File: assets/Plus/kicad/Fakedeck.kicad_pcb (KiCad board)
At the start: 2 copper layers, 118.8 x 101.5 mm, 14 parts, among them J1 Conn_01x06_Pin, J2 Conn_01x06_Pin, SW1 RotaryEncoder_Switch, SW2 RotaryEncoder_Switch, SW3 RotaryEncoder_Switch, SW4 RotaryEncoder_Switch, U1 Pico, U2 ATtiny2313-20P

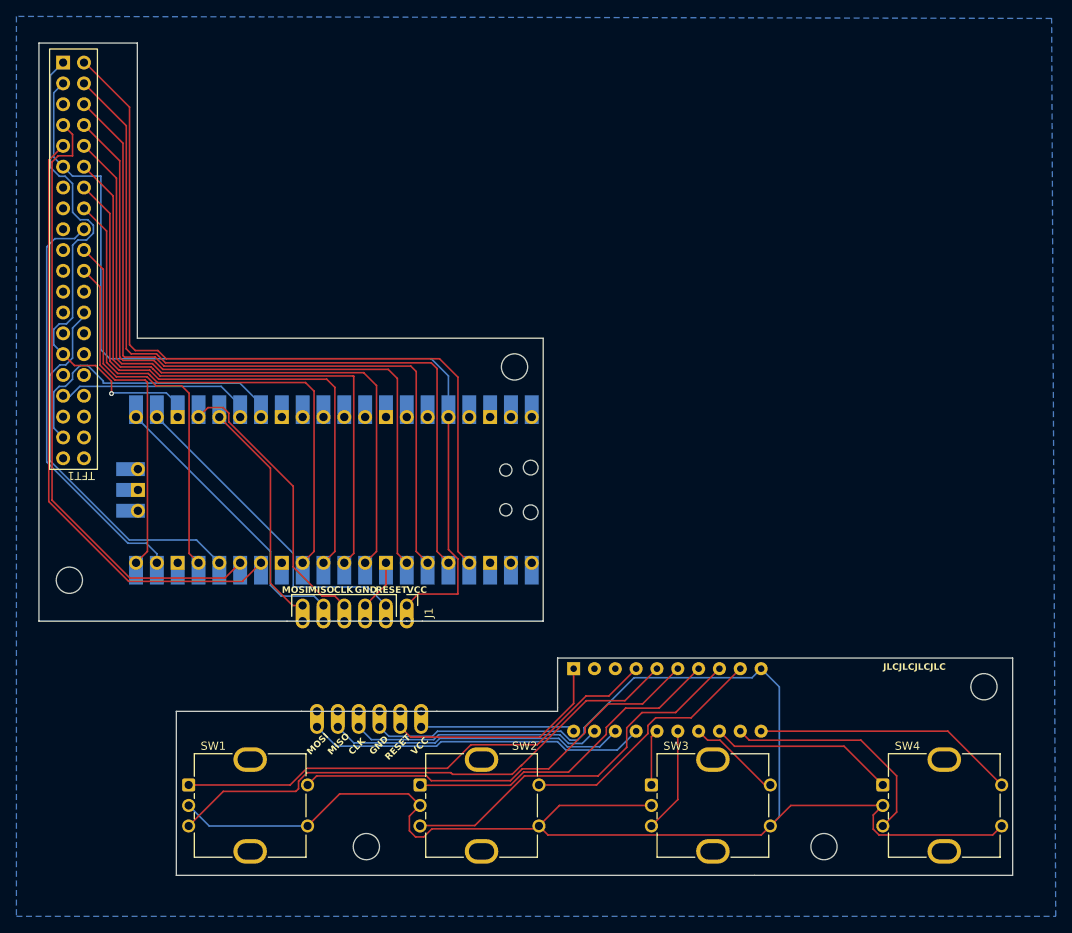
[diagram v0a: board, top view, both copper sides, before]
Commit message: Plus: Changed to connect the rotary encoder directly to the Pico. Removed the Attiny. - Updated the PCB.
 Co-Authored-By: Claude Sonnet 4.6 <noreply@anthropic.com>
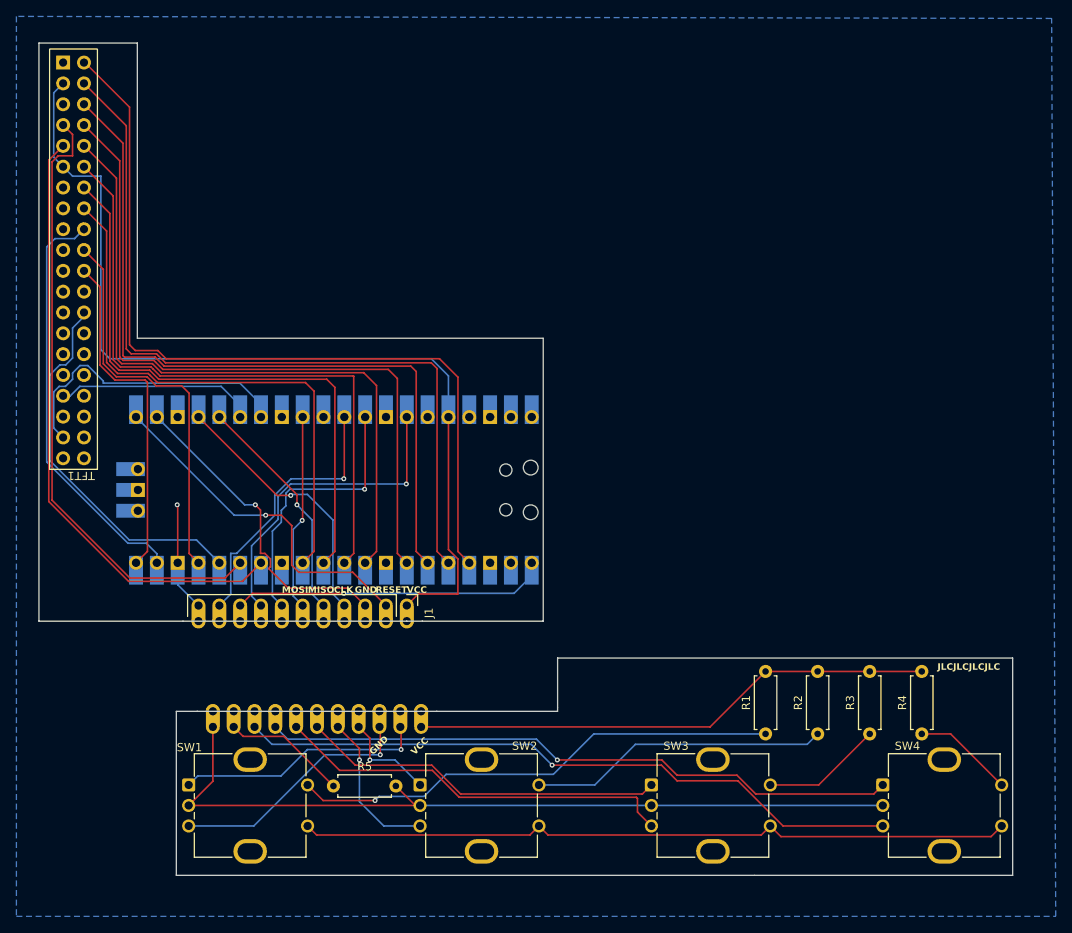
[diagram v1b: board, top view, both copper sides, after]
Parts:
- removed J2: Conn_01x06_Pin, Connector_Pin_2.54mm_Castellated:PinHeader_Castellated_1x06_P2.54mm_Vertical
- removed REF** (x5): MountingHole_3.2mm_M3, MountingHole:MountingHole_3.2mm_M3
- removed U2: ATtiny2313-20P, Package_DIP:DIP-20_W7.62mm
- added J3: Conn_01x11_Pin, Connector_Pin_2.54mm_Castellated:PinHeader_Castellated_1x11_P2.54mm_Vertical, B.Cu at (147.9, 134.4)
- added R1: 120, Resistor_THT:R_Axial_DIN0207_L6.3mm_D2.5mm_P7.62mm_Horizontal, F.Cu at (189.9, 135.3)
- added R2: 220, Resistor_THT:R_Axial_DIN0207_L6.3mm_D2.5mm_P7.62mm_Horizontal, F.Cu at (196.2, 135.3)
- added R3: 470, Resistor_THT:R_Axial_DIN0207_L6.3mm_D2.5mm_P7.62mm_Horizontal, F.Cu at (202.6, 135.3)
- added R4: 1K, Resistor_THT:R_Axial_DIN0207_L6.3mm_D2.5mm_P7.62mm_Horizontal, F.Cu at (208.9, 135.3)
- added R5: 47, Resistor_THT:R_Axial_DIN0207_L6.3mm_D2.5mm_P7.62mm_Horizontal, F.Cu at (137.2, 141.6)
- J1: value Conn_01x06_Pin -> Conn_01x11_Pin; footprint Connector_Pin_2.54mm_Castellated:PinHeader_Castellated_1x06_P2.54mm_Vertical -> Connector_Pin_2.54mm_Castellated:PinHeader_Castellated_1x11_P2.54mm_Vertical
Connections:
- J1 pad 2: /AT_RESET -> /RE1_A
- J1 pad 3: TFT_CS -> /RE1_B
- J1 pad 4: /AT_CLK -> /RE2_A
- J1 pad 5: /AT_MISO -> /RE2_B
- J1 pad 6: /AT_MOSI -> /RE3_A
- SW1 pad C: TFT_CS -> GND
- SW1 pad S1: /RE1_S -> Net-(R1-Pad1)
- SW1 pad S2: TFT_CS -> /RE_SW
- SW2 pad C: TFT_CS -> GND
- SW2 pad S1: /RE2_S -> Net-(R2-Pad1)
- SW2 pad S2: TFT_CS -> /RE_SW
- SW3 pad C: TFT_CS -> GND
- SW3 pad S1: /RE3_S -> Net-(R3-Pad1)
- SW3 pad S2: TFT_CS -> /RE_SW
- SW4 pad C: TFT_CS -> GND
- SW4 pad S1: /RE4_S -> Net-(R4-Pad1)
- SW4 pad S2: TFT_CS -> /RE_SW
- TFT1 pad 1: TFT_CS -> GND
- TFT1 pad 15: TFT_CS -> GND
- U1 pad 1: unconnected-(U1-GPIO0-Pad1) -> /RE4_B
- U1 pad 18: unconnected-(U1-GND-Pad18)_1 -> GND
- U1 pad 21: /AT_MISO -> /RE1_A
- U1 pad 22: /AT_RESET -> /RE1_B
- U1 pad 23: TFT_CS -> GND
- U1 pad 24: /AT_CLK -> /RE2_A
- U1 pad 25: /AT_MOSI -> /RE2_B
- U1 pad 29: unconnected-(U1-GPIO22-Pad29)_1 -> /RE3_A
- U1 pad 3: unconnected-(U1-GND-Pad3)_1 -> GND
- U1 pad 31: unconnected-(U1-GPIO26_ADC0-Pad31)_1 -> /RE_SW
- U1 pad 32: unconnected-(U1-GPIO27_ADC1-Pad32)_1 -> /RE3_B
- U1 pad 34: unconnected-(U1-GPIO28_ADC2-Pad34)_1 -> /RE4_A
- U1 pad 8: TFT_CS -> GND
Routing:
- net TFT_CS: track 270.7 -> 0.00 mm, vias 1 -> 0
- net /RE_SW: track 0.00 -> 136.2 mm, vias 0 -> 1
- net GND: track 0.00 -> 113.3 mm, vias 0 -> 1
- net /RE4_A: track 22.6 -> 117.5 mm, vias 0 -> 2
- net /RE4_B: track 28.1 -> 120.3 mm, vias 0 -> 2
- net /AT_MISO: track 70.9 -> 0.00 mm
- net /RE3_B: track 12.9 -> 83.1 mm, vias 0 -> 1
- net /AT_MOSI: track 69.4 -> 0.00 mm
- net /AT_RESET: track 67.5 -> 0.00 mm
- net /AT_CLK: track 65.4 -> 0.00 mm
- net /RE3_A: track 6.84 -> 68.6 mm, vias 0 -> 1
- net Net-(R1-Pad1): track 0.00 -> 60.0 mm, vias 0 -> 1
- net /RE1_S: track 51.9 -> 0.00 mm
- net TFT_RD: track 133.9 -> 178.8 mm
- net Net-(R2-Pad1): track 0.00 -> 36.6 mm
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- added copper zone on B.Cu, net GND
- removed copper zone on B.Cu, net TFT_CS
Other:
- outline, holes or cut-outs redrawn
